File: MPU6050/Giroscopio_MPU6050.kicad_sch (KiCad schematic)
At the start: 6 parts, among them U301 MPU-6050

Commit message: MPU6050: controllo delle tracce
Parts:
- added C?: 0.01uF, symbol Device:C
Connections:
- net GND: now also U301.1 (CLKIN), C?.2
- net GYRO_INT: now reaches U301.12 (INT)
- net VCC3.3: now reaches U301.8 (VDDIO)
- net VCC3.3: now also C?.1
- no-connect marks 0 -> 3
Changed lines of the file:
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@@
   (junction (at 106.68 76.2) (diameter 0) (color 0 0 0 0)
   )
+  (junction (at 88.9 91.44) (diameter 0) (color 0 0 0 0)
+  )
+  (junction (at 101.6 91.44) (diameter 0) (color 0 0 0 0)
+  )
+  (no_connect (at 120.65 81.28))
+  (no_connect (at 156.21 81.28))
+  (no_connect (at 156.21 83.82))
   (wire (pts (xy 167.64 88.9) (xy 171.45 88.9))
     (stroke (width 0) (type default) (color 0 0 0 0))
@@
     (stroke (width 0) (type default) (color 0 0 0 0))
   )
+  (wire (pts (xy 88.9 66.04) (xy 88.9 91.44))
+    (stroke (width 0) (type default) (color 0 0 0 0))
+  )
   (wire (pts (xy 148.59 62.23) (xy 151.13 62.23))
     (stroke (width 0) (type default) (color 0 0 0 0))
   )
+  (wire (pts (xy 135.89 66.04) (xy 88.9 66.04))
+    (stroke (width 0) (type default) (color 0 0 0 0))
+  )
   (wire (pts (xy 156.21 91.44) (xy 157.48 91.44))
     (stroke (width 0) (type default) (color 0 0 0 0))
   )
+  (wire (pts (xy 101.6 91.44) (xy 101.6 97.79))
+    (stroke (width 0) (type default) (color 0 0 0 0))
+  )
+  (wire (pts (xy 120.65 91.44) (xy 101.6 91.44))
+    (stroke (width 0) (type default) (color 0 0 0 0))
+  )
+  (wire (pts (xy 88.9 91.44) (xy 88.9 97.79))
+    (stroke (width 0) (type default) (color 0 0 0 0))
+  )
   (wire (pts (xy 140.97 62.23) (xy 140.97 66.04))
     (stroke (width 0) (type default) (color 0 0 0 0))
@@
     (stroke (width 0) (type default) (color 0 0 0 0))
   )
+  (wire (pts (xy 99.06 91.44) (xy 101.6 91.44))
+    (stroke (width 0) (type default) (color 0 0 0 0))
+  )
   (wire (pts (xy 157.48 99.06) (xy 157.48 100.33))
     (stroke (width 0) (type default) (color 0 0 0 0))
+  )
+  (wire (pts (xy 88.9 91.44) (xy 91.44 91.44))
+    (stroke (width 0) (type default) (color 0 0 0 0))
+  )
+  (global_label "GYRO_INT" (shape input) (at 156.21 76.2 0) (fields_autoplaced)
+    (effects (font (size 1.27 1.27)) (justify left))
+    (property "Intersheet References" "${INTERSHEET_REFS}" (id 0) (at 167.4526 76.1206 0)
+      (effects (font (size 1.27 1.27)) (justify left) hide)
+    )
+  )
+  (global_label "VCC3.3" (shape input) (at 88.9 97.79 270) (fields_autoplaced)
+    (effects (font (size 1.27 1.27)) (justify right))
+    (property "Intersheet References" "${INTERSHEET_REFS}" (id 0) (at 88.8206 106.8555 90)
+      (effects (font (size 1.27 1.27)) (justify right) hide)
+    )
   )
   (global_label "3.3v" (shape input) (at 140.97 46.99 90) (fields_autoplaced)
@@
     )
     (pin "1")
+  )
+  (symbol (lib_id "Device:C") (at 95.25 91.44 90) (unit 1)
+    (in_bom yes) (on_board yes) (fields_autoplaced)
+    (property "Reference" "C?" (id 0) (at 95.25 83.82 90))
+    (property "Value" "0.01uF" (id 1) (at 95.25 86.36 90))
+    (property "Footprint" "" (id 2) (at 99.06 90.4748 0)
+      (effects (font (size 1.27 1.27)) hide)
+    )
+    (property "Datasheet" "~" (id 3) (at 95.25 91.44 0)
+      (effects (font (size 1.27 1.27)) hide)
+    )
+    (pin "1")
+    (pin "2")
   )
   (symbol (lib_id "power:GND") (at 138.43 102.87 0) (unit 1)
@@
     (pin "1")
   )
+  (symbol (lib_id "power:GND") (at 101.6 97.79 0) (unit 1)
+    (in_bom yes) (on_board yes) (fields_autoplaced)
+    (property "Reference" "#PWR?" (id 0) (at 101.6 104.14 0)
+      (effects (font (size 1.27 1.27)) hide)
+    )
+    (property "Value" "GND" (id 1) (at 101.6 102.87 0))
+    (property "Footprint" "" (id 2) (at 101.6 97.79 0)
+      (effects (font (size 1.27 1.27)) hide)
+    )
+    (property "Datasheet" "" (id 3) (at 101.6 97.79 0)
+      (effects (font (size 1.27 1.27)) hide)
+    )
+    (pin "1")
+  )
   (sheet_instances
     (path "/" (page "1"))
@@
       (reference "#PWR0105") (unit 1) (value "GND") (footprint "")
     )
+    (path "/fe0ec9e7-1b8c-49f7-a176-18e256fdac3c"
+      (reference "#PWR?") (unit 1) (value "GND") (footprint "")
+    )
     (path "/2e251504-40fb-405f-85d7-132692c512d3"
       (reference "4.7k401") (unit 1) (value "R") (footprint "")
@@
       (reference "C403") (unit 1) (value "2200pF") (footprint "")
     )
+    (path "/8ab80e92-8330-49d2-afe4-e9d6c18b4c7b"
+      (reference "C?") (unit 1) (value "0.01uF") (footprint "")
+    )
     (path "/da7199a3-f536-4f53-8142-9e41548cc6d8"

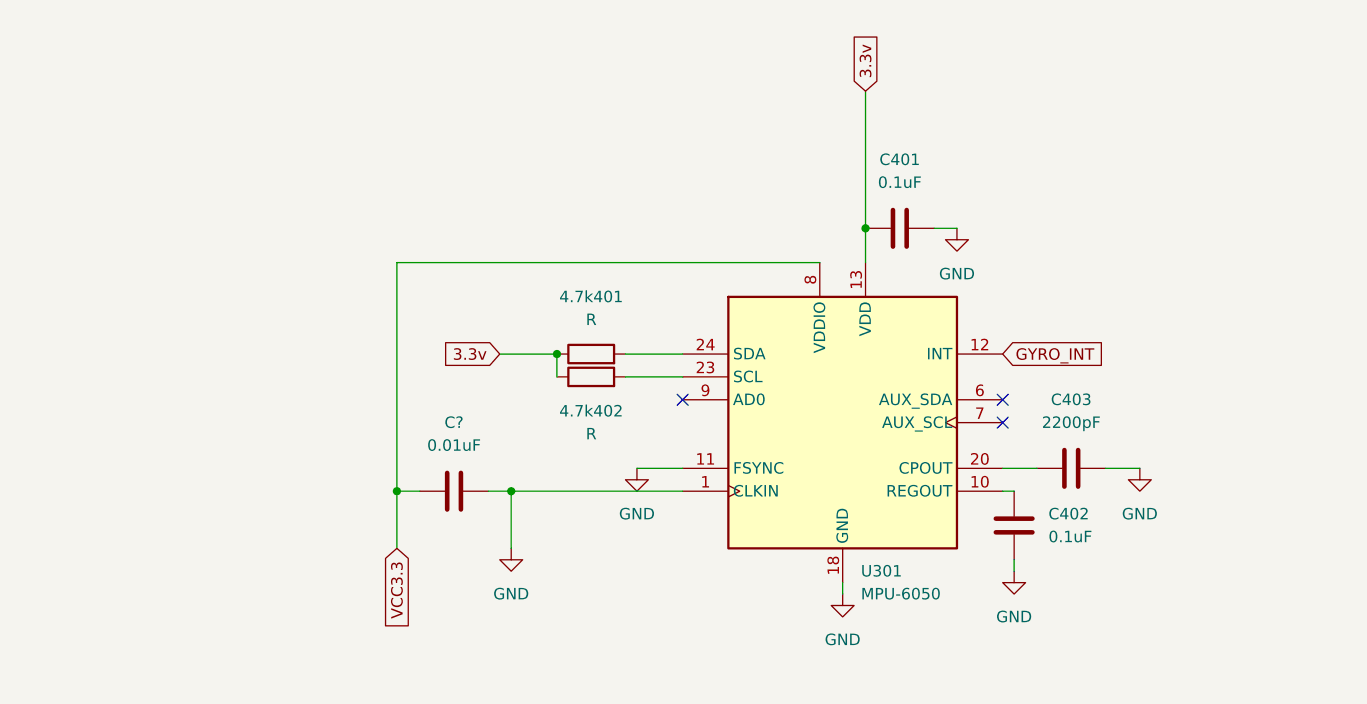
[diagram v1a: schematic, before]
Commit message: MPU6050: controllo delle tracce e riorganizzazione
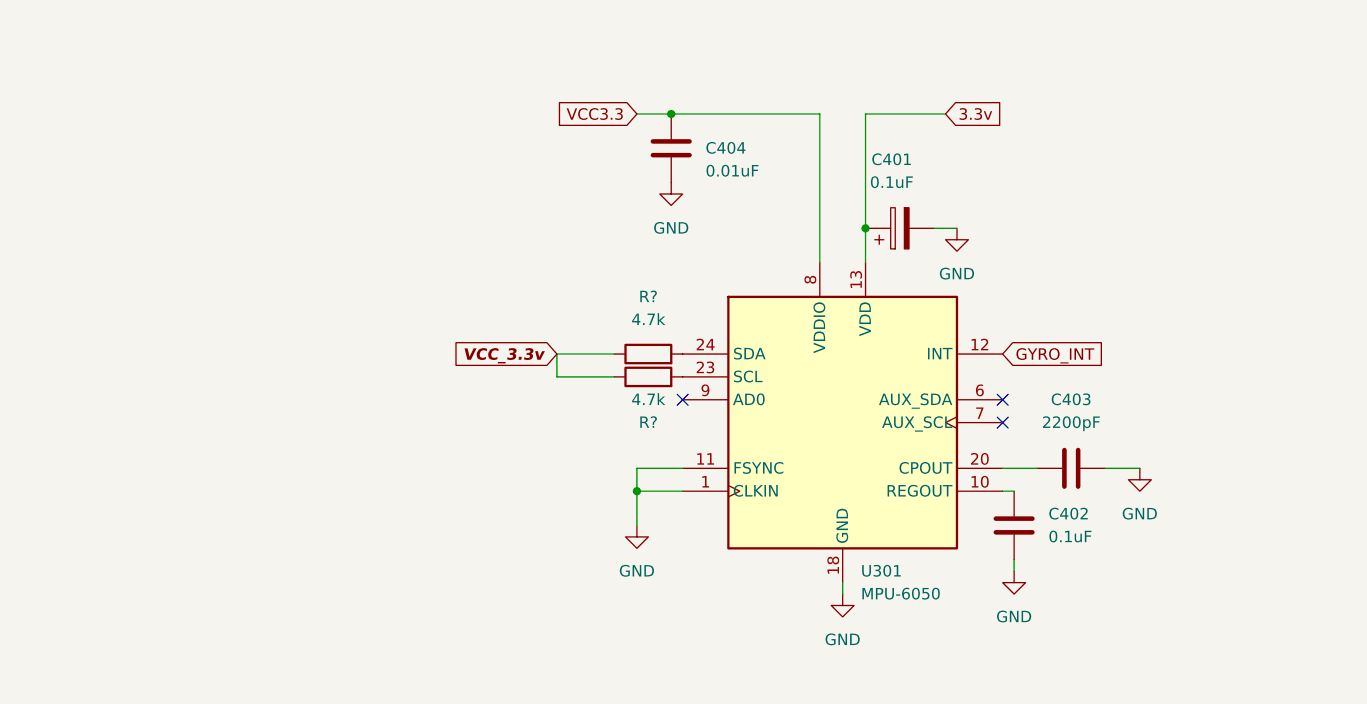
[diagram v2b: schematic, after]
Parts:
- removed 4.7k401, 4.7k402: R, symbol Device:R
- removed C401: 0.1uF, symbol Device:C
- added C401: 0.1uF, symbol Device:C_Polarized
- added R? (x2): 4.7k, symbol Device:R
- gave numbers to parts that had none: 1
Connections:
- net 3.3v: now also C401.1
- net GND: now also C404.1, C401.2; no longer C404.2
- net VCC3.3: now also C404.2; no longer C404.1
- net at U301.24 (SDA): now also R?.2
- net at U301.23 (SCL): now also R?.2
- new net VCC_3.3v: R?.1, R?.1
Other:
- moved on the sheet: C404

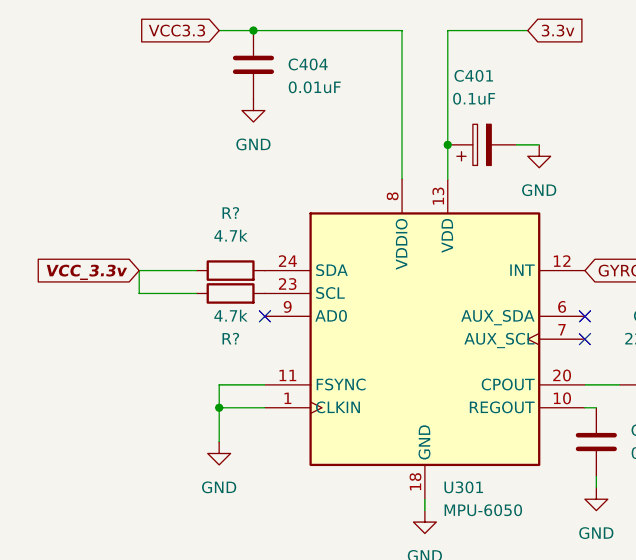
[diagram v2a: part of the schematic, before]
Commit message: MPU6050: creazione PBC
Selezionato il footprint, tirato le tracce con EdgeCuts.
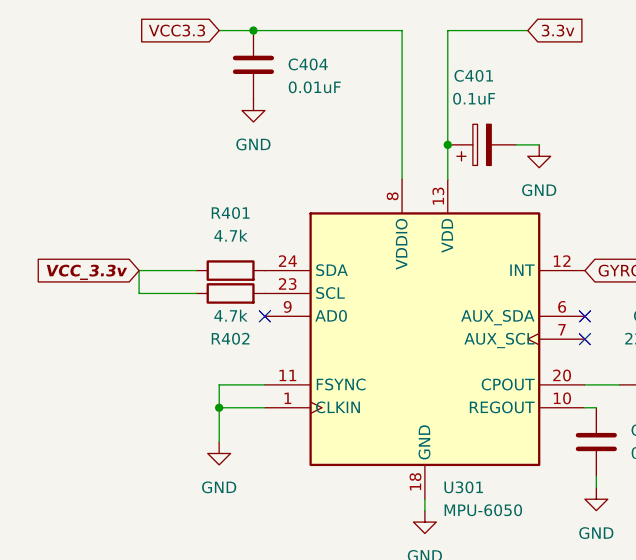
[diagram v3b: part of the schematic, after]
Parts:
- C401: footprint (none) -> Capacitor_Tantalum_SMD:CP_EIA-1608-08_AVX-J
- C402, C403, C404: footprint (none) -> Capacitor_SMD:C_0805_2012Metric
- R401, R402: renamed from R?; footprint (none) -> Resistor_SMD:R_0805_2012Metric
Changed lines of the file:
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@@
     (property "Reference" "C401" (id 0) (at 143.891 54.61 90))
     (property "Value" "0.1uF" (id 1) (at 143.891 57.15 90))
-    (property "Footprint" "" (id 2) (at 148.59 61.2648 0)
+    (property "Footprint" "Capacitor_Tantalum_SMD:CP_EIA-1608-08_AVX-J" (id 2) (at 148.59 61.2648 0)
       (effects (font (size 1.27 1.27)) hide)
     )
@@
   (symbol (lib_id "Device:R") (at 116.84 76.2 90) (unit 1)
     (in_bom yes) (on_board yes) (fields_autoplaced)
-    (property "Reference" "R?" (id 0) (at 116.84 69.85 90))
+    (property "Reference" "R401" (id 0) (at 116.84 69.85 90))
     (property "Value" "4.7k" (id 1) (at 116.84 72.39 90))
-    (property "Footprint" "" (id 2) (at 116.84 77.978 90)
+    (property "Footprint" "Resistor_SMD:R_0805_2012Metric" (id 2) (at 116.84 77.978 90)
       (effects (font (size 1.27 1.27)) hide)
     )
@@
     (property "Reference" "C403" (id 0) (at 163.83 81.28 90))
     (property "Value" "2200pF" (id 1) (at 163.83 83.82 90))
-    (property "Footprint" "" (id 2) (at 167.64 87.9348 0)
+    (property "Footprint" "Capacitor_SMD:C_0805_2012Metric" (id 2) (at 167.64 87.9348 0)
       (effects (font (size 1.27 1.27)) hide)
     )
@@
   (symbol (lib_id "power:GND") (at 119.38 57.15 0) (unit 1)
     (in_bom yes) (on_board yes) (fields_autoplaced)
-    (property "Reference" "#PWR?" (id 0) (at 119.38 63.5 0)
+    (property "Reference" "#PWR0401" (id 0) (at 119.38 63.5 0)
       (effects (font (size 1.27 1.27)) hide)
     )
@@
       (effects (font (size 1.27 1.27)) (justify right))
     )
-    (property "Footprint" "" (id 2) (at 118.4148 49.53 0)
+    (property "Footprint" "Capacitor_SMD:C_0805_2012Metric" (id 2) (at 118.4148 49.53 0)
       (effects (font (size 1.27 1.27)) hide)
     )
@@
       (effects (font (size 1.27 1.27)) (justify left))
     )
-    (property "Footprint" "" (id 2) (at 158.4452 99.06 0)
+    (property "Footprint" "Capacitor_SMD:C_0805_2012Metric" (id 2) (at 158.4452 99.06 0)
       (effects (font (size 1.27 1.27)) hide)
     )
@@
   (symbol (lib_id "Device:R") (at 116.84 78.74 90) (unit 1)
     (in_bom yes) (on_board yes)
-    (property "Reference" "R?" (id 0) (at 116.84 83.82 90))
+    (property "Reference" "R402" (id 0) (at 116.84 83.82 90))
     (property "Value" "4.7k" (id 1) (at 116.84 81.28 90))
-    (property "Footprint" "" (id 2) (at 116.84 80.518 90)
+    (property "Footprint" "Resistor_SMD:R_0805_2012Metric" (id 2) (at 116.84 80.518 90)
       (effects (font (size 1.27 1.27)) hide)
     )
@@
     )
     (path "/825cc6b8-f8c7-47b8-8227-0f9b7ac0b3d9"
-      (reference "#PWR?") (unit 1) (value "GND") (footprint "")
+      (reference "#PWR0401") (unit 1) (value "GND") (footprint "")
     )
     (path "/1ca5e19a-e1ad-483a-a5a7-3aaf6b67b377"
-      (reference "C401") (unit 1) (value "0.1uF") (footprint "")
+      (reference "C401") (unit 1) (value "0.1uF") (footprint "Capacitor_Tantalum_SMD:CP_EIA-1608-08_AVX-J")
     )
     (path "/9b047bc1-0203-4b51-9939-6f7c5b0d22c4"
-      (reference "C402") (unit 1) (value "0.1uF") (footprint "")
+      (reference "C402") (unit 1) (value "0.1uF") (footprint "Capacitor_SMD:C_0805_2012Metric")
     )
     (path "/719e2d86-e50e-4472-aa02-ffcb840f9afa"
-      (reference "C403") (unit 1) (value "2200pF") (footprint "")
+      (reference "C403") (unit 1) (value "2200pF") (footprint "Capacitor_SMD:C_0805_2012Metric")
     )
     (path "/8ab80e92-8330-49d2-afe4-e9d6c18b4c7b"
-      (reference "C404") (unit 1) (value "0.01uF") (footprint "")
+      (reference "C404") (unit 1) (value "0.01uF") (footprint "Capacitor_SMD:C_0805_2012Metric")
     )
     (path "/4a776592-badf-4679-907a-201ed16a7491"
-      (reference "R?") (unit 1) (value "4.7k") (footprint "")
+      (reference "R401") (unit 1) (value "4.7k") (footprint "Resistor_SMD:R_0805_2012Metric")
     )
     (path "/d5a7e300-55b8-468e-bbcc-872093ed3c8c"
-      (reference "R?") (unit 1) (value "4.7k") (footprint "")
+      (reference "R402") (unit 1) (value "4.7k") (footprint "Resistor_SMD:R_0805_2012Metric")
     )
     (path "/da7199a3-f536-4f53-8142-9e41548cc6d8"

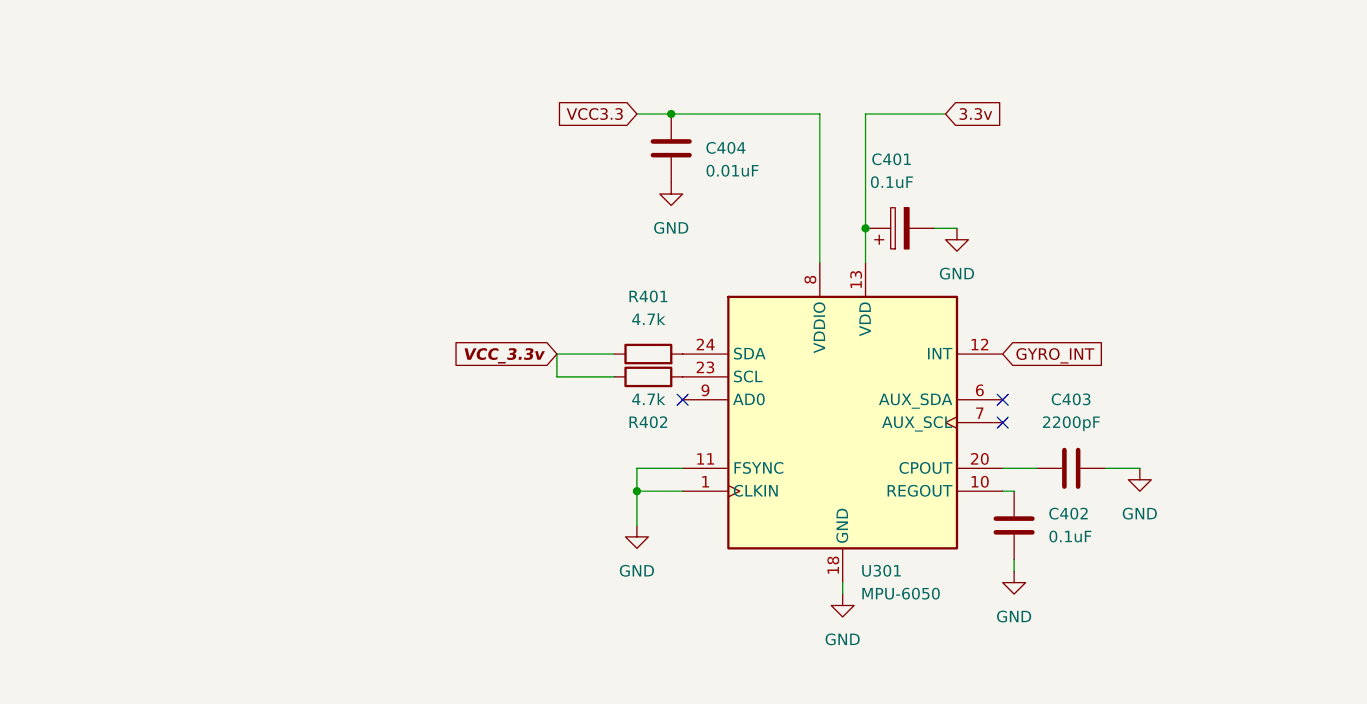
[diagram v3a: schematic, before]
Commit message: MPU6050: aggiornamento della schematica
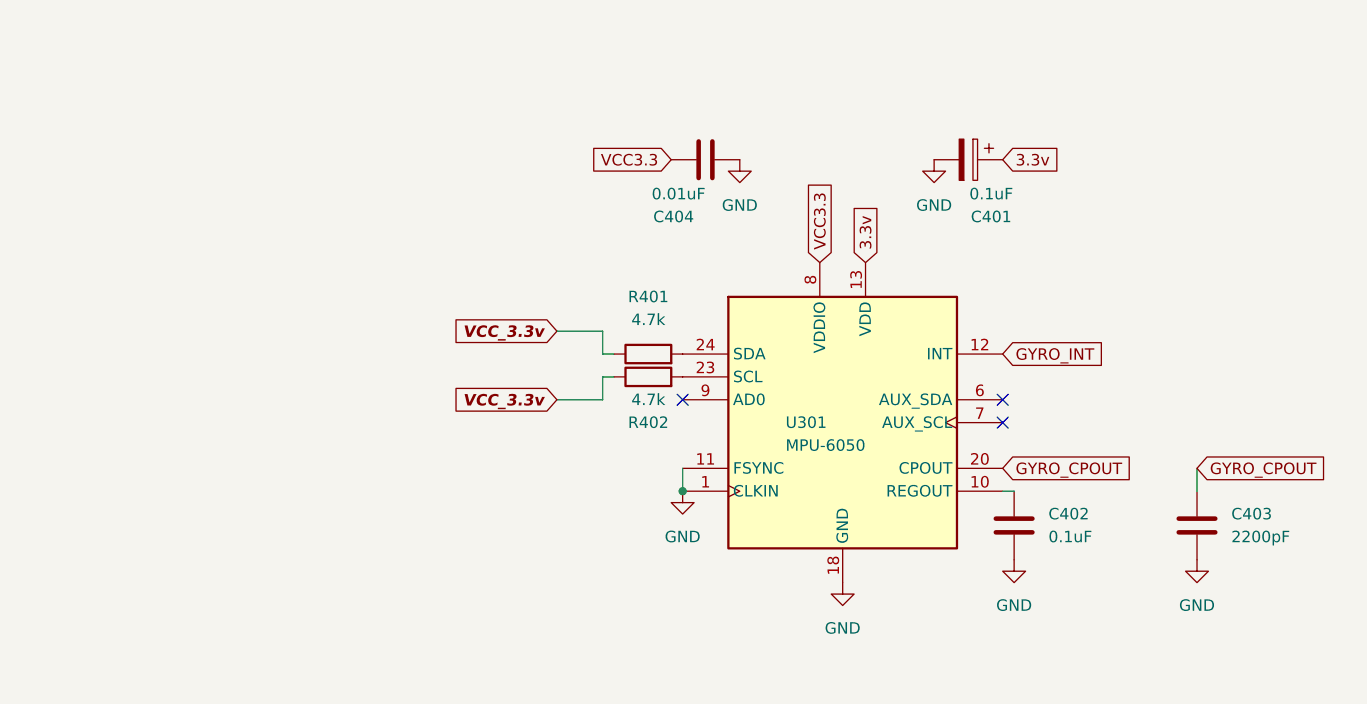
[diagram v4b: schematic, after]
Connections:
- net GND: now also C403.1; no longer C403.2
- net GYRO_CPOUT: now reaches U301.20 (CPOUT)
- net GYRO_CPOUT: now also C403.2; no longer C403.1
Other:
- moved on the sheet: C401, C403, C404
